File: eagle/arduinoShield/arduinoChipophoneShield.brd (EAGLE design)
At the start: 101.6 x 53.3 mm, 29 parts

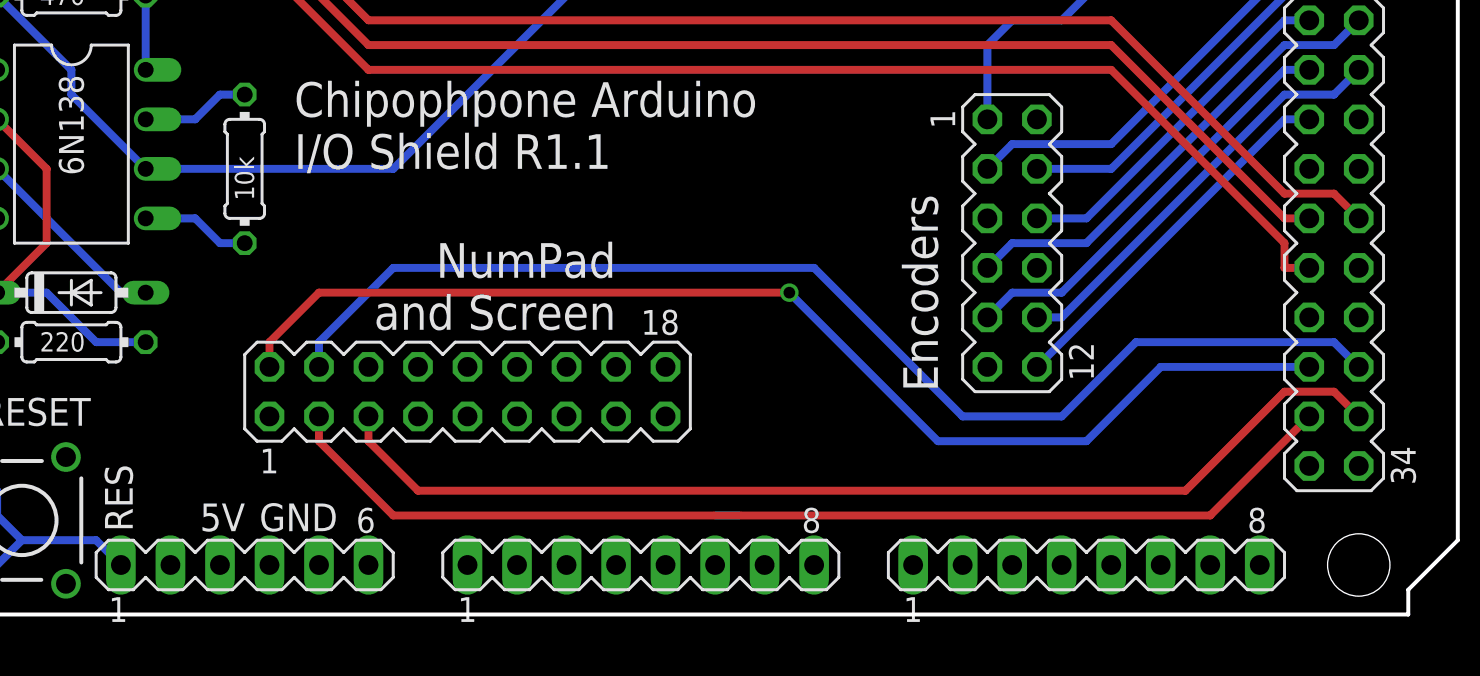
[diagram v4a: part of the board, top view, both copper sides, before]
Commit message: Updated to R1.2, which fixes the missing Pin on the screen header. Also has CS connected now too
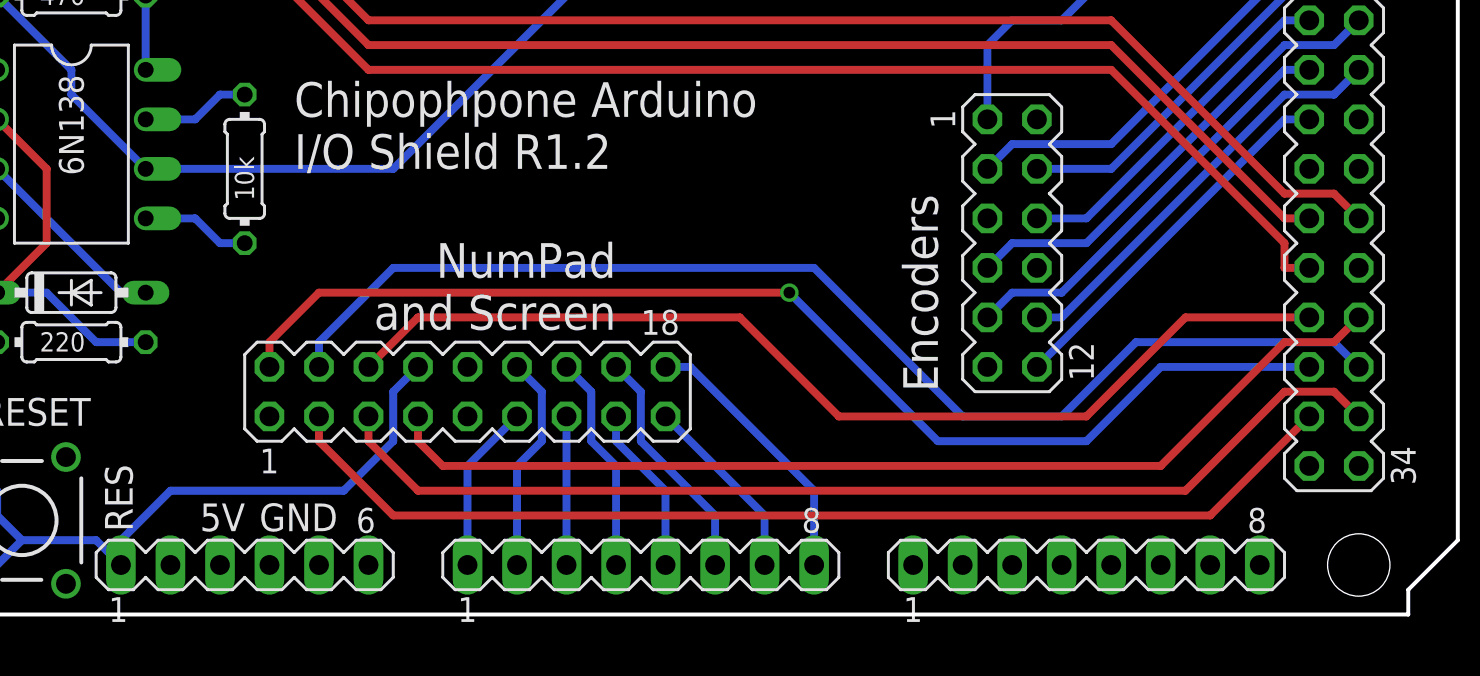
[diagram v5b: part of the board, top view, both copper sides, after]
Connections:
- net A5 renamed N$9
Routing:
- net D48: track 0.00 -> 53.5 mm
- net D49: track 0.00 -> 53.2 mm
- net RES: track 17.9 -> 39.6 mm
- net A7: track 0.00 -> 14.1 mm
- net N$9: track 1.27 -> 13.5 mm
- net A3: track 1.27 -> 12.5 mm
- net A1: track 0.00 -> 11.2 mm
- net A0: track 0.00 -> 8.67 mm
- net A4: track 1.27 -> 9.94 mm
- net A6: track 2.54 -> 11.0 mm
- net A2: track 1.27 -> 8.89 mm
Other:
- board text added: "Chipophpone Arduino I/O Shield R1.2"
- board text removed: "Chipophpone Arduino I/O Shield R1.1"
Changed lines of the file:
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@@
 <text x="2.54" y="50.8" size="1.778" layer="21">MIDI Out</text>
 <text x="41.91" y="22.86" size="1.778" layer="21">Chipophpone Arduino
-I/O Shield R1.1</text>
+I/O Shield R1.2</text>
 <hole x="15.24" y="50.8" drill="3.2"/>
 <text x="20.32" y="27.94" size="1.27" layer="21" rot="R180">+</text>
@@
 <wire x1="26.67" y1="6.35" x2="25.4" y2="7.62" width="0.4064" layer="16"/>
 <contactref element="SCREEN_NUMPAD" pad="8"/>
-<wire x1="33.02" y1="2.54" x2="48.26" y2="12.7" width="0" layer="19" extent="1-1"/>
+<wire x1="33.02" y1="2.54" x2="33.02" y2="3.81" width="0.4064" layer="16"/>
+<wire x1="33.02" y1="3.81" x2="35.56" y2="6.35" width="0.4064" layer="16"/>
+<wire x1="35.56" y1="6.35" x2="44.45" y2="6.35" width="0.4064" layer="16"/>
+<wire x1="44.45" y1="6.35" x2="46.99" y2="8.89" width="0.4064" layer="16"/>
+<wire x1="46.99" y1="8.89" x2="46.99" y2="11.43" width="0.4064" layer="16"/>
+<wire x1="46.99" y1="11.43" x2="48.26" y2="12.7" width="0.4064" layer="16"/>
+<wire x1="25.4" y1="7.62" x2="25.6794" y2="8.0772" width="0" layer="19" extent="16-16"/>
 <wire x1="22.86" y1="5.461" x2="22.86" y2="5.08" width="0" layer="19" extent="16-16"/>
 <wire x1="25.6794" y1="1.5748" x2="25.4" y2="1.27" width="0" layer="19" extent="16-16"/>
-<wire x1="25.6794" y1="8.0772" x2="25.4" y2="7.62" width="0" layer="19" extent="16-16"/>
 </signal>
 <signal name="5V">
@@
 <contactref element="JP1" pad="1"/>
 <contactref element="SCREEN_NUMPAD" pad="11"/>
-<wire x1="50.8" y1="2.54" x2="53.34" y2="10.16" width="0" layer="19" extent="1-1"/>
+<wire x1="50.8" y1="2.54" x2="50.8" y2="7.62" width="0.4064" layer="16"/>
+<wire x1="50.8" y1="7.62" x2="53.34" y2="10.16" width="0.4064" layer="16"/>
 </signal>
 <signal name="A1">
 <contactref element="JP1" pad="2"/>
 <contactref element="SCREEN_NUMPAD" pad="12"/>
-<wire x1="53.34" y1="2.54" x2="53.34" y2="12.7" width="0" layer="19" extent="1-1"/>
+<wire x1="53.34" y1="2.54" x2="53.34" y2="7.62" width="0.4064" layer="16"/>
+<wire x1="53.34" y1="7.62" x2="54.61" y2="8.89" width="0.4064" layer="16"/>
+<wire x1="54.61" y1="8.89" x2="54.61" y2="11.43" width="0.4064" layer="16"/>
+<wire x1="54.61" y1="11.43" x2="53.34" y2="12.7" width="0.4064" layer="16"/>
 </signal>
 <signal name="A2">
@@
 <contactref element="JP1" pad="3"/>
 <contactref element="SCREEN_NUMPAD" pad="13"/>
-<wire x1="55.88" y1="3.81" x2="55.88" y2="10.16" width="0" layer="19" extent="16-16"/>
+<wire x1="55.88" y1="2.54" x2="55.88" y2="10.16" width="0.4064" layer="16"/>
 </signal>
 <signal name="A3">
@@
 <contactref element="JP1" pad="4"/>
 <contactref element="SCREEN_NUMPAD" pad="14"/>
-<wire x1="58.42" y1="3.81" x2="55.88" y2="12.7" width="0" layer="19" extent="16-16"/>
+<wire x1="58.42" y1="2.54" x2="58.42" y2="7.62" width="0.4064" layer="16"/>
+<wire x1="58.42" y1="7.62" x2="57.15" y2="8.89" width="0.4064" layer="16"/>
+<wire x1="57.15" y1="8.89" x2="57.15" y2="11.43" width="0.4064" layer="16"/>
+<wire x1="57.15" y1="11.43" x2="55.88" y2="12.7" width="0.4064" layer="16"/>
 </signal>
 <signal name="A4">
@@
 <contactref element="JP1" pad="5"/>
 <contactref element="SCREEN_NUMPAD" pad="15"/>
-<wire x1="60.96" y1="3.81" x2="58.42" y2="10.16" width="0" layer="19" extent="16-16"/>
-</signal>
-<signal name="A5">
-<wire x1="63.5" y1="3.81" x2="63.5" y2="2.54" width="0.4064" layer="16"/>
-<contactref element="JP1" pad="6"/>
-<contactref element="SCREEN_NUMPAD" pad="16"/>
-<wire x1="63.5" y1="3.81" x2="58.42" y2="12.7" width="0" layer="19" extent="16-16"/>
+<wire x1="60.96" y1="2.54" x2="60.96" y2="6.35" width="0.4064" layer="16"/>
+<wire x1="60.96" y1="6.35" x2="58.42" y2="8.89" width="0.4064" layer="16"/>
+<wire x1="58.42" y1="8.89" x2="58.42" y2="10.16" width="0.4064" layer="16"/>
 </signal>
 <signal name="A6">
-<wire x1="63.5" y1="5.08" x2="64.77" y2="5.08" width="0.4064" layer="16"/>
 <wire x1="66.04" y1="3.81" x2="66.04" y2="2.54" width="0.4064" layer="16"/>
 <contactref element="JP1" pad="7"/>
 <contactref element="SCREEN_NUMPAD" pad="17"/>
-<wire x1="63.5" y1="5.08" x2="60.96" y2="10.16" width="0" layer="19" extent="16-16"/>
-<wire x1="66.04" y1="3.81" x2="64.77" y2="5.08" width="0" layer="19" extent="16-16"/>
+<wire x1="66.04" y1="2.54" x2="66.04" y2="5.08" width="0.4064" layer="16"/>
+<wire x1="66.04" y1="5.08" x2="60.96" y2="10.16" width="0.4064" layer="16"/>
 </signal>
 <signal name="A7">
 <contactref element="JP1" pad="8"/>
 <contactref element="SCREEN_NUMPAD" pad="18"/>
-<wire x1="68.58" y1="2.54" x2="60.96" y2="12.7" width="0" layer="19" extent="1-1"/>
+<wire x1="60.96" y1="12.7" x2="62.23" y2="12.7" width="0.4064" layer="16"/>
+<wire x1="62.23" y1="12.7" x2="68.58" y2="6.35" width="0.4064" layer="16"/>
+<wire x1="68.58" y1="6.35" x2="68.58" y2="2.54" width="0.4064" layer="16"/>
 </signal>
 <signal name="A8">
@@
 <contactref element="SV1" pad="27"/>
 <contactref element="SCREEN_NUMPAD" pad="6"/>
-<wire x1="45.72" y1="12.7" x2="93.98" y2="15.24" width="0" layer="19" extent="1-1"/>
+<wire x1="93.98" y1="15.24" x2="87.63" y2="15.24" width="0.4064" layer="1"/>
+<wire x1="87.63" y1="15.24" x2="82.55" y2="10.16" width="0.4064" layer="1"/>
+<wire x1="82.55" y1="10.16" x2="69.85" y2="10.16" width="0.4064" layer="1"/>
+<wire x1="69.85" y1="10.16" x2="64.77" y2="15.24" width="0.4064" layer="1"/>
+<wire x1="64.77" y1="15.24" x2="48.26" y2="15.24" width="0.4064" layer="1"/>
+<wire x1="48.26" y1="15.24" x2="45.72" y2="12.7" width="0.4064" layer="1"/>
 </signal>
 <signal name="D41">
@@
 <contactref element="SV1" pad="28"/>
 <contactref element="SCREEN_NUMPAD" pad="7"/>
-<wire x1="48.26" y1="10.16" x2="96.52" y2="15.24" width="0" layer="19" extent="1-1"/>
+<wire x1="48.26" y1="10.16" x2="48.26" y2="8.89" width="0.4064" layer="1"/>
+<wire x1="48.26" y1="8.89" x2="49.53" y2="7.62" width="0.4064" layer="1"/>
+<wire x1="49.53" y1="7.62" x2="86.36" y2="7.62" width="0.4064" layer="1"/>
+<wire x1="86.36" y1="7.62" x2="92.71" y2="13.97" width="0.4064" layer="1"/>
+<wire x1="92.71" y1="13.97" x2="95.25" y2="13.97" width="0.4064" layer="1"/>
+<wire x1="95.25" y1="13.97" x2="96.52" y2="15.24" width="0.4064" layer="1"/>
 </signal>
 <signal name="3.3">
@@
 <wire x1="22.86" y1="30.48" x2="22.86" y2="25.4" width="0.4064" layer="1"/>
 </signal>
+<signal name="N$9">
+<wire x1="63.5" y1="5.08" x2="59.69" y2="8.89" width="0.4064" layer="16"/>
+<wire x1="59.69" y1="8.89" x2="59.69" y2="11.43" width="0.4064" layer="16"/>
+<wire x1="63.5" y1="3.81" x2="63.5" y2="2.54" width="0.4064" layer="16"/>
+<contactref element="JP1" pad="6"/>
+<contactref element="SCREEN_NUMPAD" pad="16"/>
+<wire x1="59.69" y1="11.43" x2="58.42" y2="12.7" width="0.4064" layer="16"/>
+<wire x1="63.5" y1="5.08" x2="63.5" y2="2.54" width="0.4064" layer="16"/>
+</signal>
 </signals>

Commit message: Updated to R1.3, correct RX/TX pins. Not that I'm going to reprint it, but for good measure...
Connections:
- net D18: now also MIDI_OUT.5
- net D19: now also OK1.6, R7.1
- net RX0: no longer OK1.6, R7.1
- net TX1: no longer MIDI_OUT.5
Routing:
- net D19: track 0.00 -> 82.8 mm, vias 0 -> 1
- net D18: track 0.00 -> 67.4 mm
- net RX0: track 59.5 -> 0.00 mm
- net TX1: track 49.6 -> 1.27 mm
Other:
- board text added: "Chipophpone Arduino I/O Shield R1.3"
- board text removed: "Chipophpone Arduino I/O Shield R1.2"
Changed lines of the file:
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@@
 <text x="2.54" y="50.8" size="1.778" layer="21">MIDI Out</text>
 <text x="41.91" y="22.86" size="1.778" layer="21">Chipophpone Arduino
-I/O Shield R1.2</text>
+I/O Shield R1.3</text>
 <hole x="15.24" y="50.8" drill="3.2"/>
 <text x="20.32" y="27.94" size="1.27" layer="21" rot="R180">+</text>
@@
 <signal name="D18">
 <contactref element="JP5" pad="4"/>
+<contactref element="MIDI_OUT" pad="5"/>
+<wire x1="15.24" y1="45.72" x2="17.78" y2="48.26" width="0.4064" layer="1"/>
+<wire x1="17.78" y1="48.26" x2="24.13" y2="48.26" width="0.4064" layer="1"/>
+<wire x1="24.13" y1="48.26" x2="25.4" y2="46.99" width="0.4064" layer="1"/>
+<wire x1="25.4" y1="46.99" x2="72.39" y2="46.99" width="0.4064" layer="1"/>
+<wire x1="72.39" y1="46.99" x2="73.66" y2="48.26" width="0.4064" layer="1"/>
+<wire x1="73.66" y1="48.26" x2="77.47" y2="48.26" width="0.4064" layer="1"/>
+<wire x1="77.47" y1="48.26" x2="78.74" y2="49.53" width="0.4064" layer="1"/>
+<wire x1="78.74" y1="49.53" x2="78.74" y2="50.8" width="0.4064" layer="1"/>
 </signal>
 <signal name="D19">
 <contactref element="JP5" pad="3"/>
-</signal>
-<signal name="SDA">
-<contactref element="JP5" pad="2"/>
-</signal>
-<signal name="SCL">
-<contactref element="JP5" pad="1"/>
-</signal>
-<signal name="RX0">
-<contactref element="JP4" pad="1"/>
 <contactref element="OK1" pad="6"/>
 <contactref element="R7" pad="1"/>
-<wire x1="63.5" y1="50.8" x2="63.5" y2="39.37" width="0.4064" layer="16"/>
-<wire x1="63.5" y1="39.37" x2="46.99" y2="22.86" width="0.4064" layer="16"/>
-<wire x1="46.99" y1="22.86" x2="34.29" y2="22.86" width="0.4064" layer="16"/>
 <wire x1="34.29" y1="22.86" x2="30.48" y2="26.67" width="0.4064" layer="16"/>
 <wire x1="30.48" y1="26.67" x2="30.48" y2="27.94" width="0.4064" layer="16"/>
 <wire x1="30.48" y1="27.94" x2="26.67" y2="31.75" width="0.4064" layer="16"/>
+<wire x1="81.28" y1="50.8" x2="81.28" y2="49.53" width="0.4064" layer="1"/>
+<wire x1="81.28" y1="49.53" x2="82.55" y2="48.26" width="0.4064" layer="1"/>
+<wire x1="82.55" y1="48.26" x2="82.55" y2="33.02" width="0.4064" layer="1"/>
+<wire x1="82.55" y1="33.02" x2="81.28" y2="31.75" width="0.4064" layer="1"/>
+<wire x1="81.28" y1="31.75" x2="57.15" y2="31.75" width="0.4064" layer="1"/>
+<via x="57.15" y="31.75" extent="1-16" drill="0.6" shape="square"/>
+<wire x1="34.29" y1="22.86" x2="46.99" y2="22.86" width="0.4064" layer="16"/>
+<wire x1="46.99" y1="22.86" x2="55.88" y2="31.75" width="0.4064" layer="16"/>
+<wire x1="55.88" y1="31.75" x2="57.15" y2="31.75" width="0.4064" layer="16"/>
+</signal>
+<signal name="SDA">
+<contactref element="JP5" pad="2"/>
+</signal>
+<signal name="SCL">
+<contactref element="JP5" pad="1"/>
+</signal>
+<signal name="RX0">
+<contactref element="JP4" pad="1"/>
 </signal>
 <signal name="TX1">
 <contactref element="JP4" pad="2"/>
-<contactref element="MIDI_OUT" pad="5"/>
 <wire x1="60.96" y1="50.8" x2="60.96" y2="49.53" width="0.4064" layer="1"/>
-<wire x1="60.96" y1="49.53" x2="58.42" y2="46.99" width="0.4064" layer="1"/>
-<wire x1="58.42" y1="46.99" x2="25.4" y2="46.99" width="0.4064" layer="1"/>
-<wire x1="25.4" y1="46.99" x2="24.13" y2="48.26" width="0.4064" layer="1"/>
-<wire x1="24.13" y1="48.26" x2="17.78" y2="48.26" width="0.4064" layer="1"/>
-<wire x1="17.78" y1="48.26" x2="15.24" y2="45.72" width="0.4064" layer="1"/>
 </signal>
 <signal name="AREF">

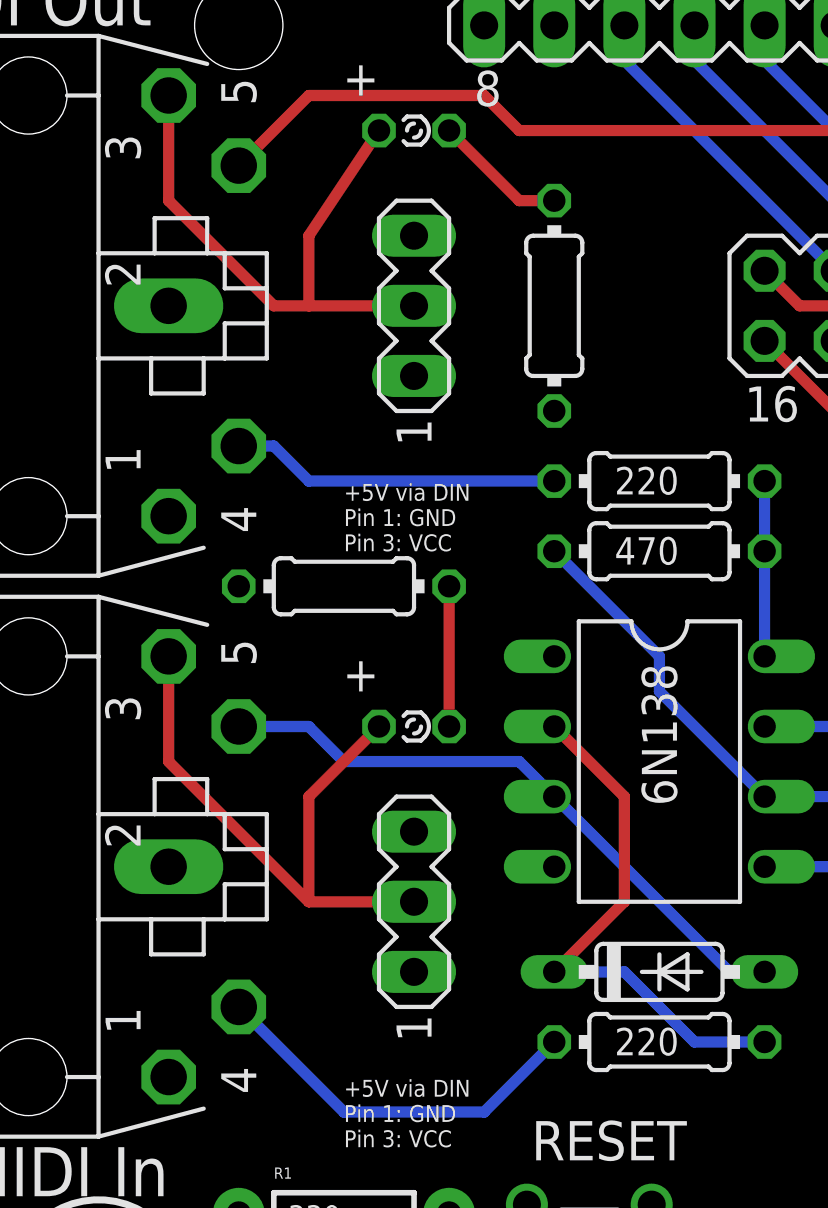
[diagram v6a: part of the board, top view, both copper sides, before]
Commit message: Switched the switches around so ON points to the LED, makes more sense that way.
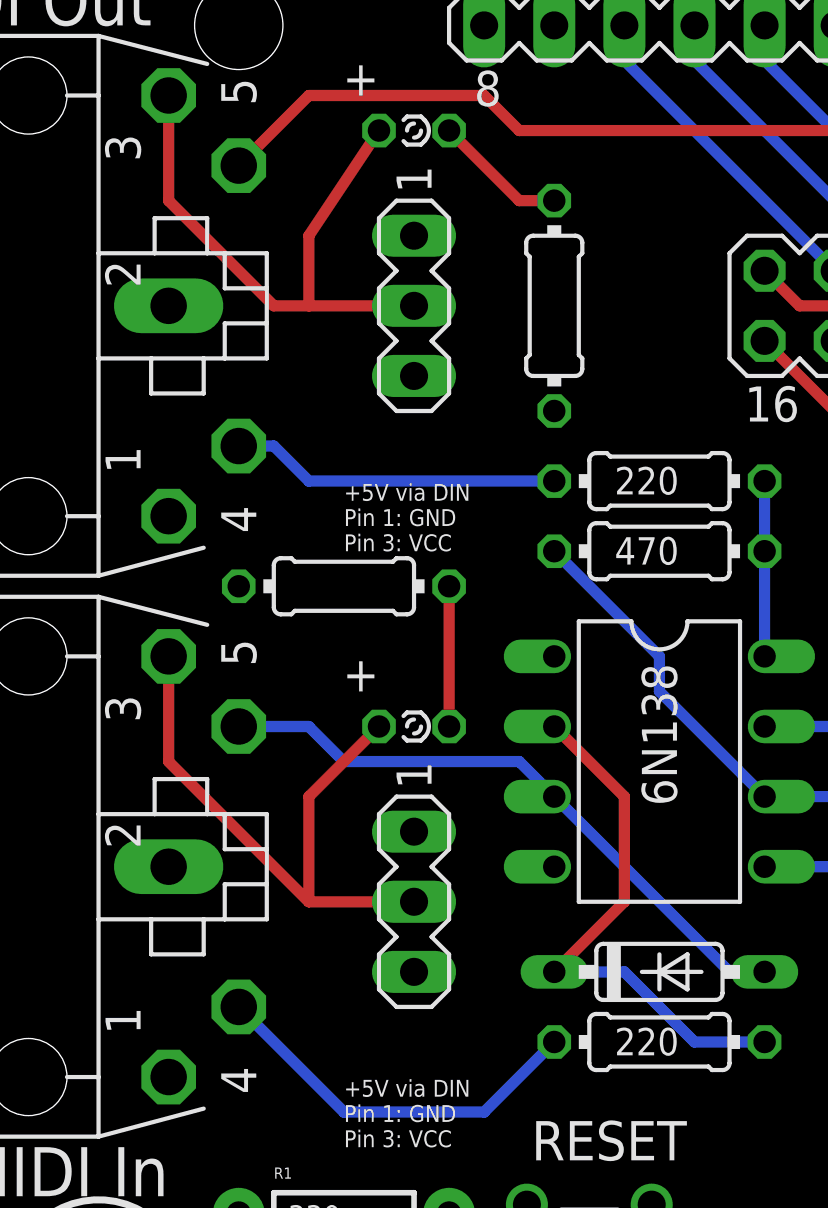
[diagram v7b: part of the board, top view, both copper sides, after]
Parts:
- turned SV3 to 270 degrees
- turned SV4 to 270 degrees
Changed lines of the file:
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@@
 </element>
 <element name="D1" library="diode" package="DO35-7" value="1N4148DO35-7" x="30.48" y="16.51" smashed="yes"/>
-<element name="SV3" library="con-lstb" package="MA03-1" value="" x="21.59" y="40.64" smashed="yes" rot="R90">
-<attribute name="OC_NEWARK" value="unknown" x="21.59" y="40.64" size="1.27" layer="27" rot="R90" display="off"/>
-<attribute name="MPN" value="" x="21.59" y="40.64" size="1.27" layer="27" rot="R90" display="off"/>
-<attribute name="MF" value="" x="21.59" y="40.64" size="1.27" layer="27" rot="R90" display="off"/>
-<attribute name="OC_FARNELL" value="unknown" x="21.59" y="40.64" size="1.27" layer="27" rot="R90" display="off"/>
-<attribute name="VALUE" x="24.511" y="36.83" size="1.27" layer="27" ratio="10" rot="R90"/>
+<element name="SV3" library="con-lstb" package="MA03-1" value="" x="21.59" y="40.64" smashed="yes" rot="R270">
+<attribute name="OC_NEWARK" value="unknown" x="21.59" y="40.64" size="1.27" layer="27" rot="R270" display="off"/>
+<attribute name="MPN" value="" x="21.59" y="40.64" size="1.27" layer="27" rot="R270" display="off"/>
+<attribute name="MF" value="" x="21.59" y="40.64" size="1.27" layer="27" rot="R270" display="off"/>
+<attribute name="OC_FARNELL" value="unknown" x="21.59" y="40.64" size="1.27" layer="27" rot="R270" display="off"/>
+<attribute name="VALUE" x="18.669" y="44.45" size="1.27" layer="27" ratio="10" rot="R270"/>
 </element>
-<element name="SV4" library="con-lstb" package="MA03-1" value="" x="21.59" y="19.05" smashed="yes" rot="R90">
-<attribute name="OC_NEWARK" value="unknown" x="21.59" y="19.05" size="1.27" layer="27" rot="R90" display="off"/>
-<attribute name="MPN" value="" x="21.59" y="19.05" size="1.27" layer="27" rot="R90" display="off"/>
-<attribute name="MF" value="" x="21.59" y="19.05" size="1.27" layer="27" rot="R90" display="off"/>
-<attribute name="OC_FARNELL" value="unknown" x="21.59" y="19.05" size="1.27" layer="27" rot="R90" display="off"/>
-<attribute name="VALUE" x="24.511" y="15.24" size="1.27" layer="27" ratio="10" rot="R90"/>
+<element name="SV4" library="con-lstb" package="MA03-1" value="" x="21.59" y="19.05" smashed="yes" rot="R270">
+<attribute name="OC_NEWARK" value="unknown" x="21.59" y="19.05" size="1.27" layer="27" rot="R270" display="off"/>
+<attribute name="MPN" value="" x="21.59" y="19.05" size="1.27" layer="27" rot="R270" display="off"/>
+<attribute name="MF" value="" x="21.59" y="19.05" size="1.27" layer="27" rot="R270" display="off"/>
+<attribute name="OC_FARNELL" value="unknown" x="21.59" y="19.05" size="1.27" layer="27" rot="R270" display="off"/>
+<attribute name="VALUE" x="18.669" y="22.86" size="1.27" layer="27" ratio="10" rot="R270"/>
 </element>
 <element name="LED2" library="led" package="LSU260" value="" x="21.59" y="46.99" smashed="yes">
